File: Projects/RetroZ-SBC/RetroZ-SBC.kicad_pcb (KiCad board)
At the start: 2 copper layers, 127 x 73.7 mm, 59 parts, among them IC1 PO_RESET, IC2 AT28C256B-15PU, IC3 AS6C62256-55PCN, J1 02x20, J2 01x08, J3 01x08, J4 PARENT INT. SEL., J5 USB_OTG, J6 CLOCK DIV., J7 PSW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

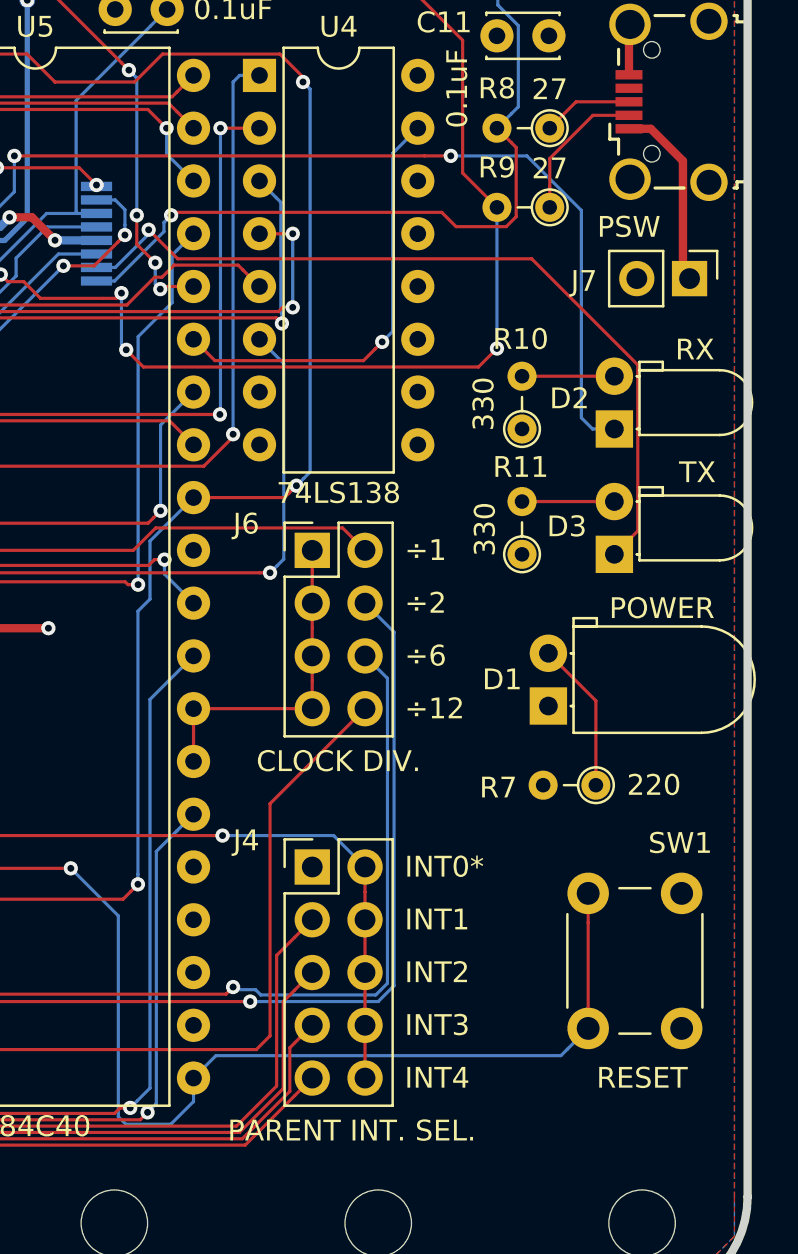
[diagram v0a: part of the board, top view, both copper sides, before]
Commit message: added a dip switch to toggle the computer power
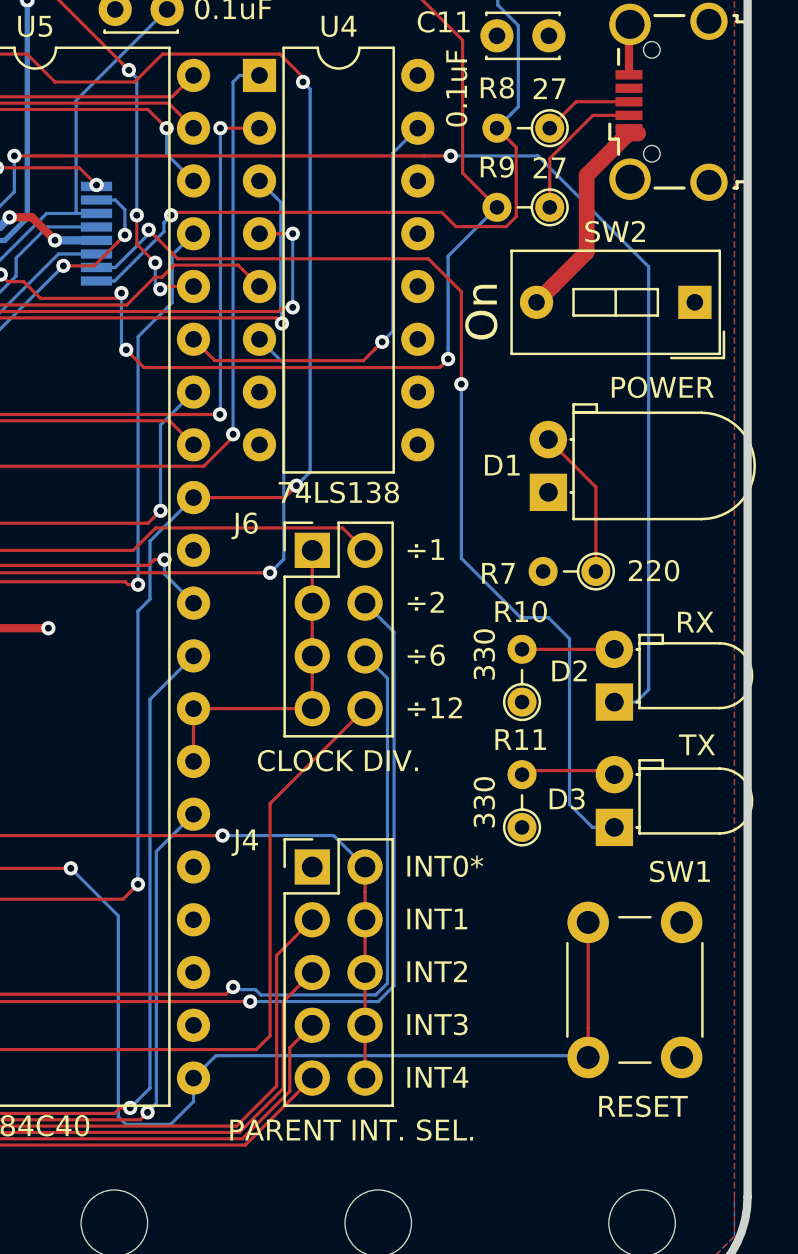
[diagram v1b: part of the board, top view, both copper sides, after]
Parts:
- removed J7: PSW, Pin_Headers:Pin_Header_Straight_1x02_Pitch2.54mm
- added SW2: POWER SWITCH, Buttons_Switches_THT:SW_DIP_x1_W7.62mm_Slide, F.Cu at (210.8, 91.6)
- moved D2 13.1 mm to (206.9, 110.8)
- moved D3 13.1 mm to (206.9, 116.8)
- moved R10 13.1 mm to (202.5, 110.8)
- moved R11 13.1 mm to (202.5, 116.8)
- moved D1 10.3 mm to (203.8, 100.7)
- moved R7 10.3 mm to (206.1, 104.5)
- moved SW1 1.40 mm to (210.2, 121.4)
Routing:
- net Net-(D2-Pad1): track 44.3 -> 59.1 mm
- net Net-(D3-Pad1): track 39.2 -> 49.9 mm, vias 1 -> 2
- net Net-(J5-Pad1): track 9.03 -> 12.9 mm
- net Net-(C3-Pad1): track 49.5 -> 48.4 mm
- net /~RESET: track 196.2 -> 195.7 mm
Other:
- board text added: "On"

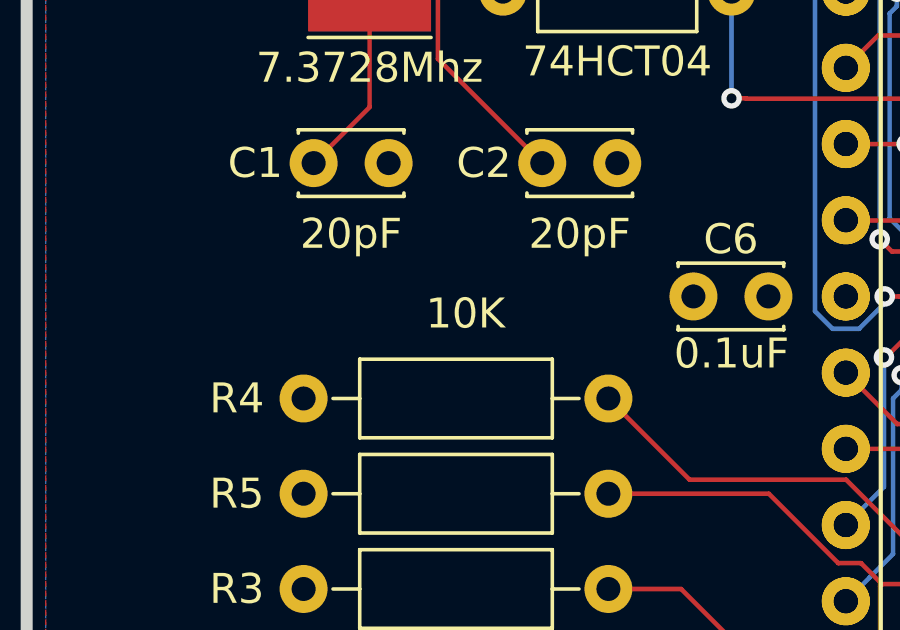
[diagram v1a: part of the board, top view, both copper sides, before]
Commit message: updated readme.md and some schematic texts
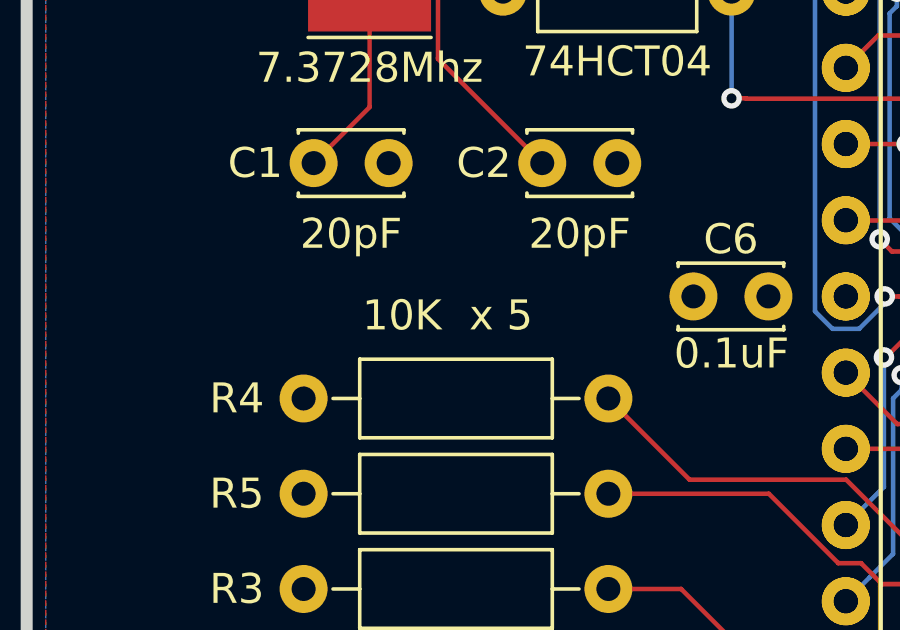
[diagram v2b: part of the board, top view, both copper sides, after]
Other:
- board text added: "x 5"

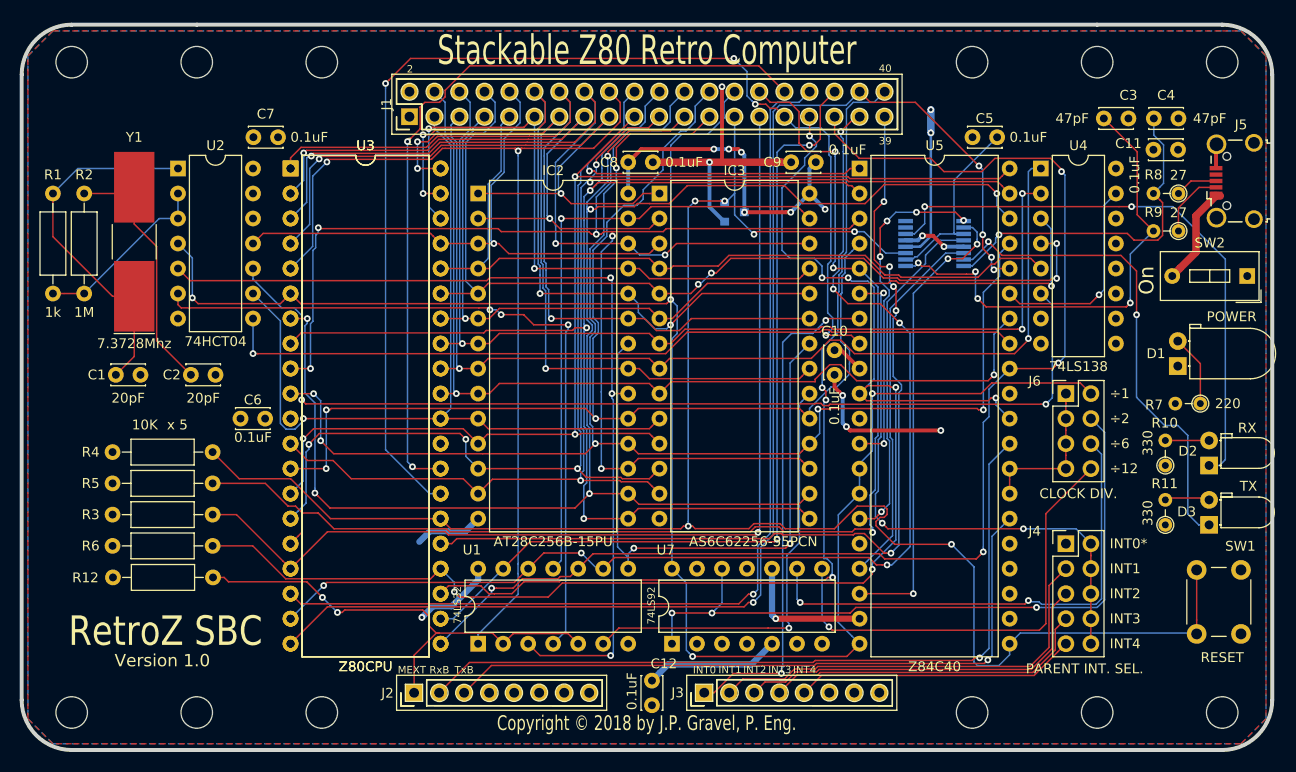
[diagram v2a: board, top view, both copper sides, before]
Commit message: moved some high speed signals traces away from other traces
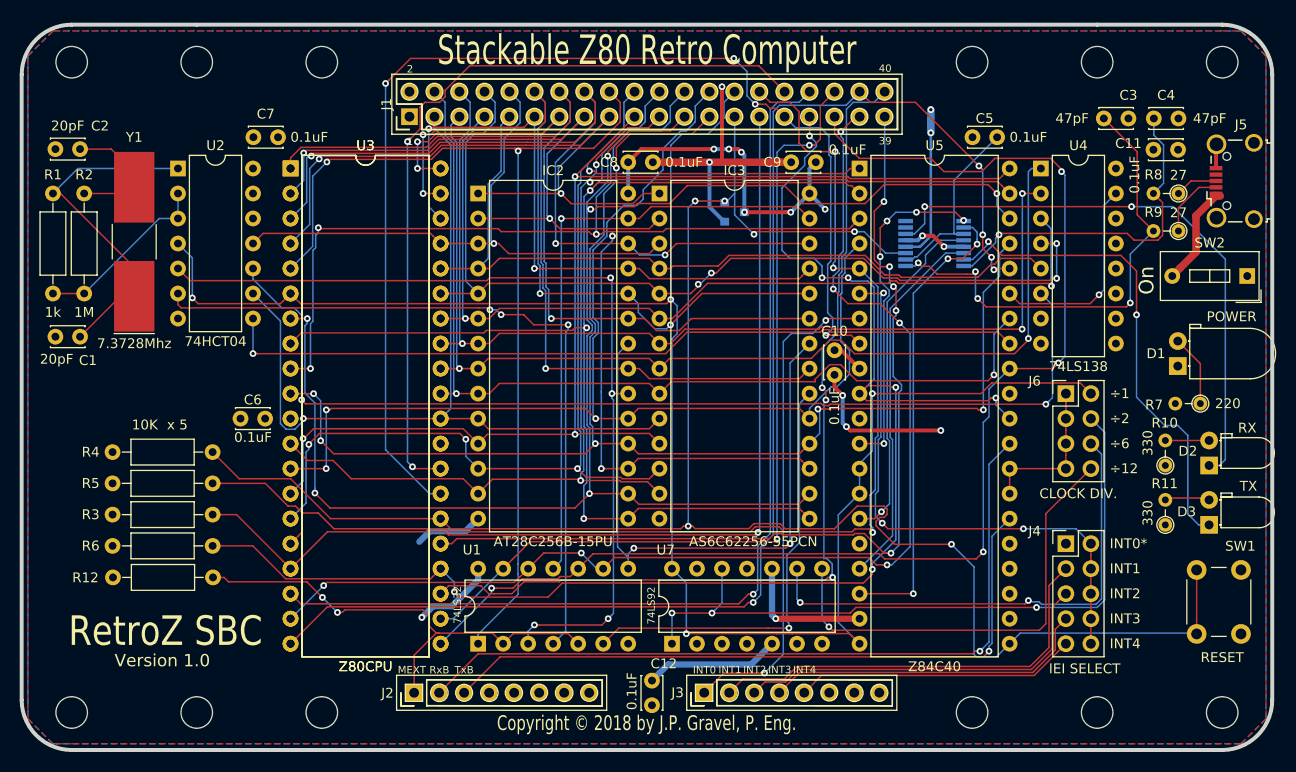
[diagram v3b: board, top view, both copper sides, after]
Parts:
- J4: value PARENT INT. SEL. -> IEI SELECT
- moved C2 25.5 mm to (92.3, 78.7), turned to 180 degrees
- moved C1 5.31 mm to (92.3, 97.7), turned to 180 degrees
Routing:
- net Net-(C2-Pad1): track 26.8 -> 13.3 mm
- net /ROM_SEL: track 93.7 -> 91.1 mm, vias 3 -> 4
- net Net-(C1-Pad1): track 37.6 -> 35.3 mm
- net /~CLK: track 187.2 -> 185.2 mm
- net /~RESET: track 195.7 -> 193.8 mm
- net /INT_0: track 51.1 -> 50.1 mm
